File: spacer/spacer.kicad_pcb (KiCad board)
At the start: 2 copper layers, 21.5 x 3.2 mm, 1 part

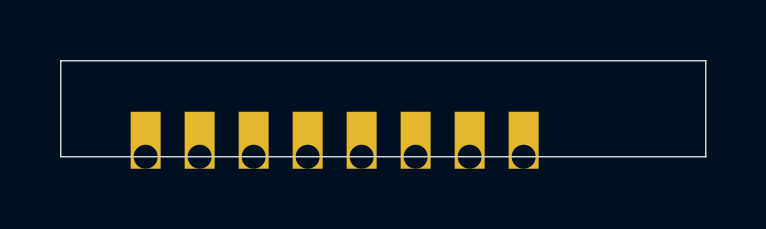
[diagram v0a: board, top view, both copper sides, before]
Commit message: spacer: height to 3.1mm
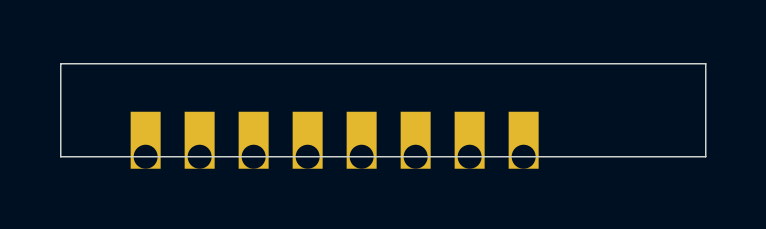
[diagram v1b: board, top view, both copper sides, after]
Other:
- board size 21.5 x 3.2 mm -> 21.5 x 3.1 mm
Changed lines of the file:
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@@
     (pad "8" thru_hole rect (at 4.68 0) (size 1 1.9) (drill 0.8 (offset 0 -0.55)) (layers *.Cu *.Mask))
   )
-  (gr_line (start -10.75 0) (end -10.75 -3.2) (layer "Edge.Cuts") (width 0.05))
-  (gr_line (start 10.75 -3.2) (end -10.75 -3.2) (layer "Edge.Cuts") (width 0.05))
-  (gr_line (start 10.75 0) (end 10.75 -3.2) (layer "Edge.Cuts") (width 0.05))
+  (gr_line (start -10.75 0) (end -10.75 -3.1) (layer "Edge.Cuts") (width 0.05))
+  (gr_line (start 10.75 -3.1) (end -10.75 -3.1) (layer "Edge.Cuts") (width 0.05))
+  (gr_line (start 10.75 0) (end 10.75 -3.1) (layer "Edge.Cuts") (width 0.05))
   (gr_line (start -10.75 0) (end 10.75 0) (layer "Edge.Cuts") (width 0.05))
 )
